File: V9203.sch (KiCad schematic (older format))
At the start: 80 parts, among them J1 RJ45, J10 GS3, J4 Screw_Terminal_1x04, J6 CONN_01X09, J7 GS3, J8 GS3, U1 V9203, Y1 Crystal_GND24

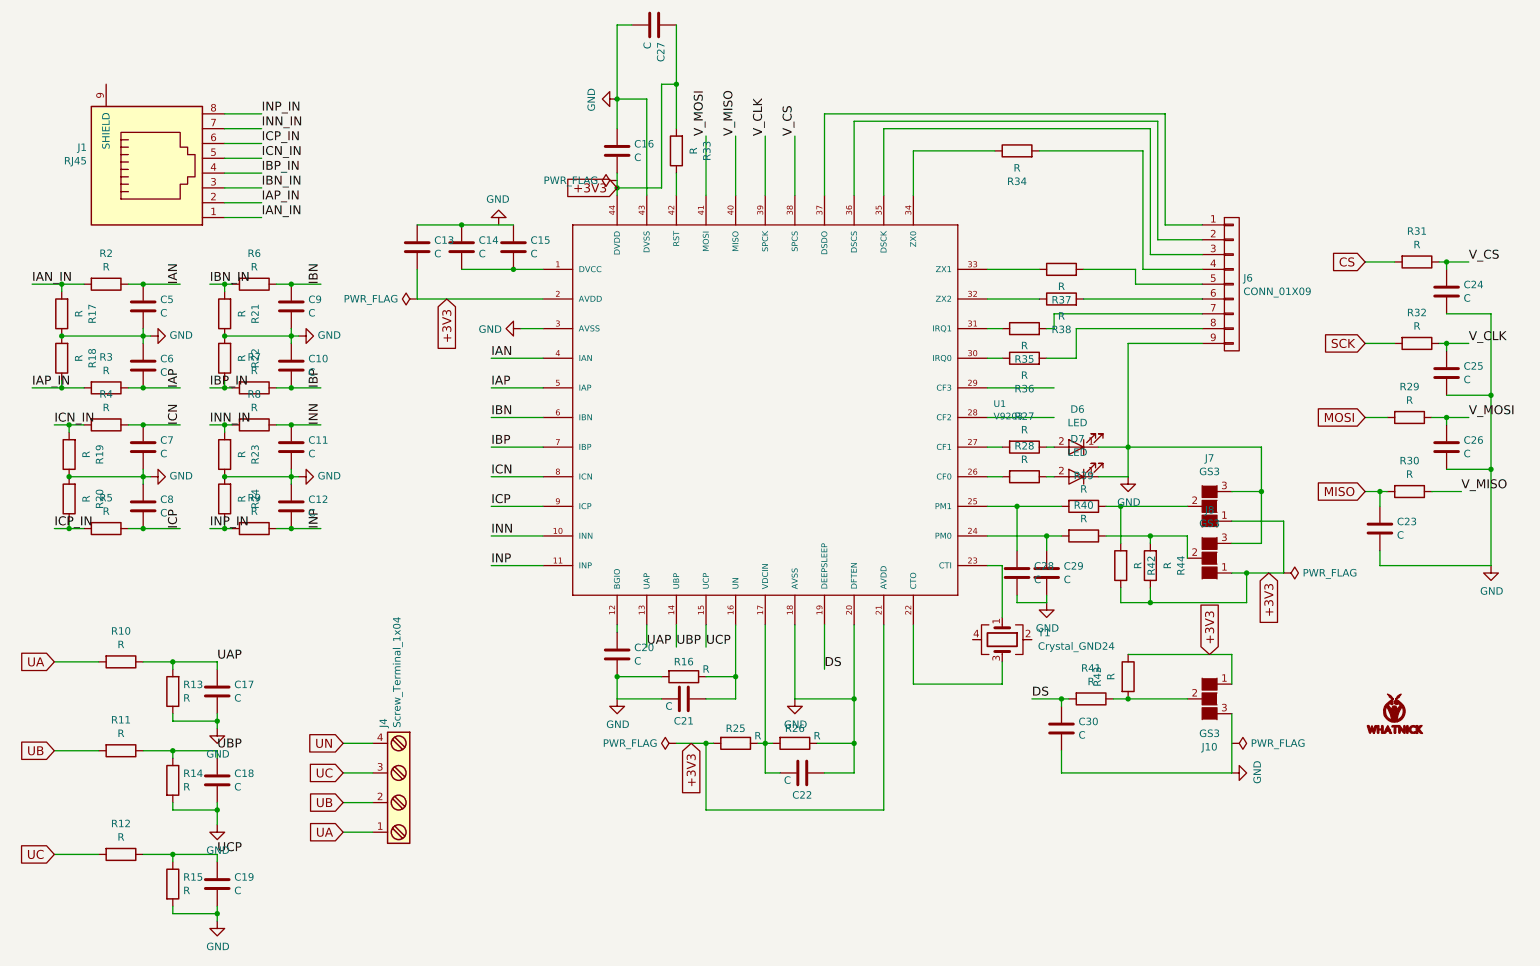
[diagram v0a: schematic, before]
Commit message: Ran ERC and updated pcb
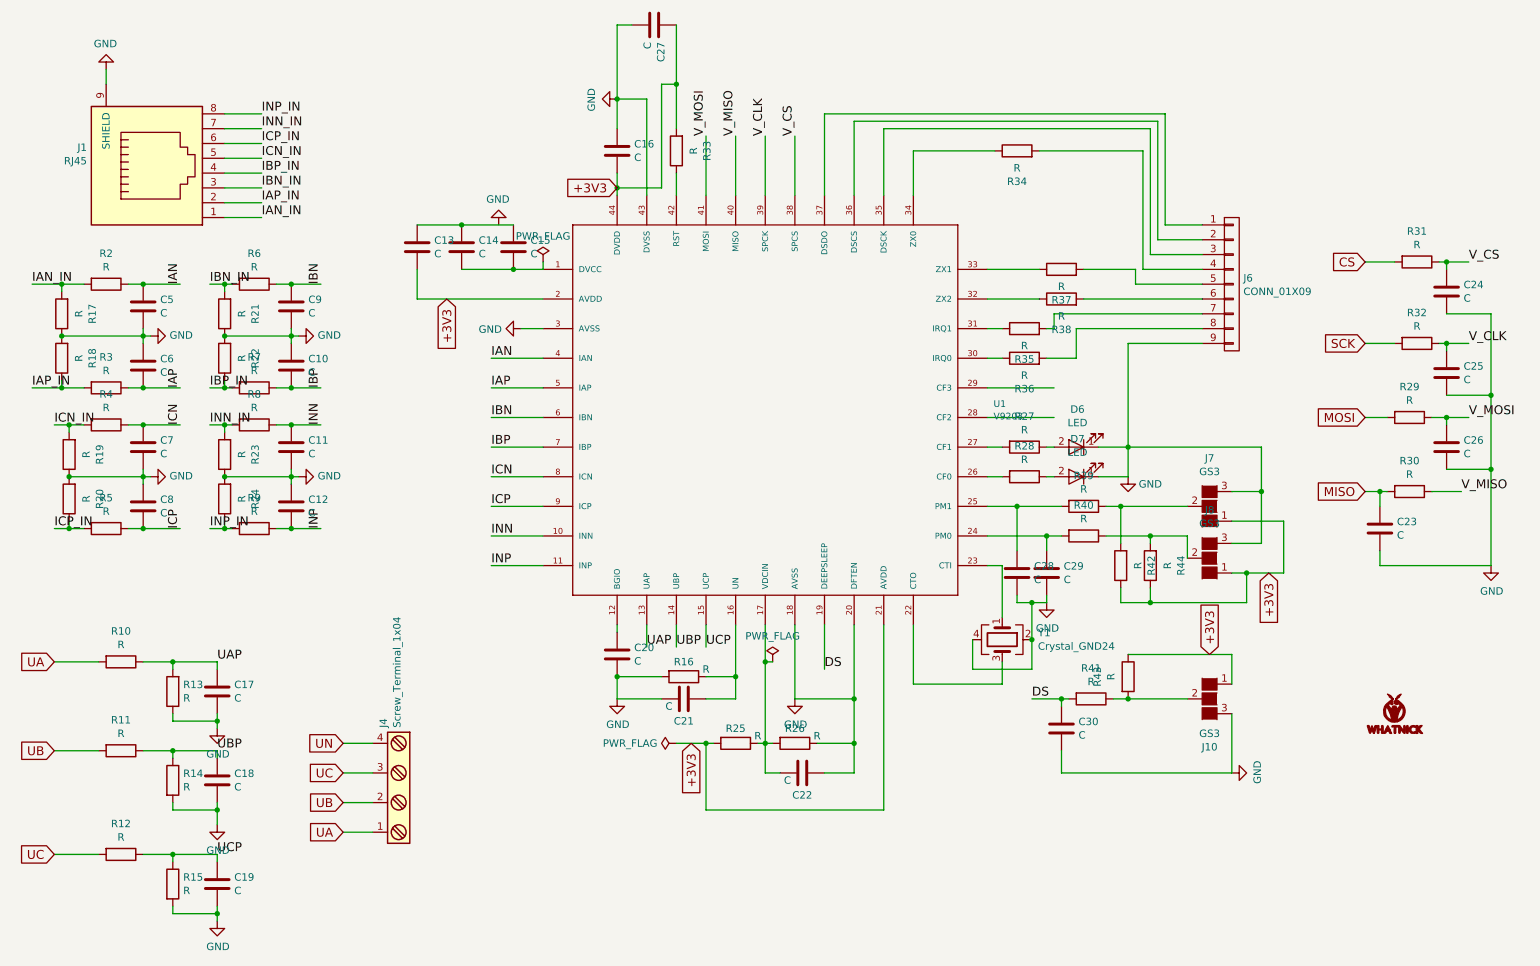
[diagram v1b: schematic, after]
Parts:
- LOGO2: footprint (none) -> Whatnick_logo:Whatnick_logo
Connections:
- net GND: now also J1.9 (SHIELD), Y1.2, Y1.4

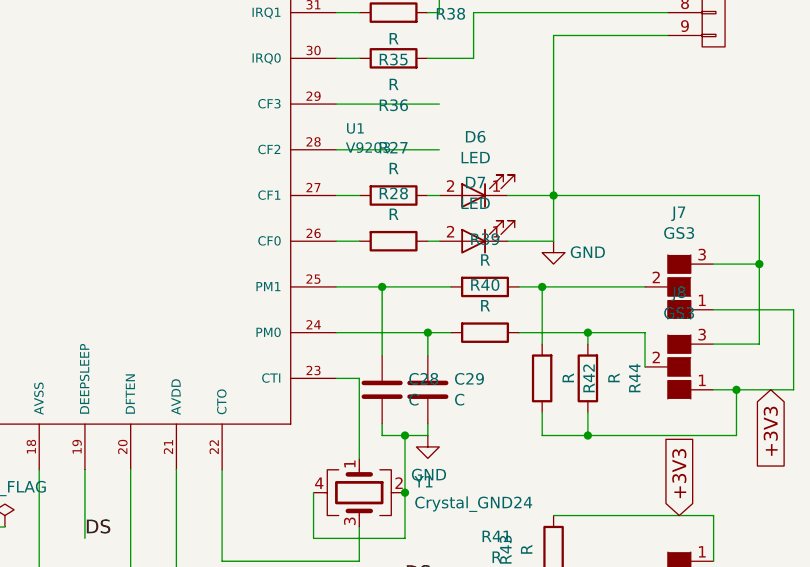
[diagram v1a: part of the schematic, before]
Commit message: Added silk screen markers
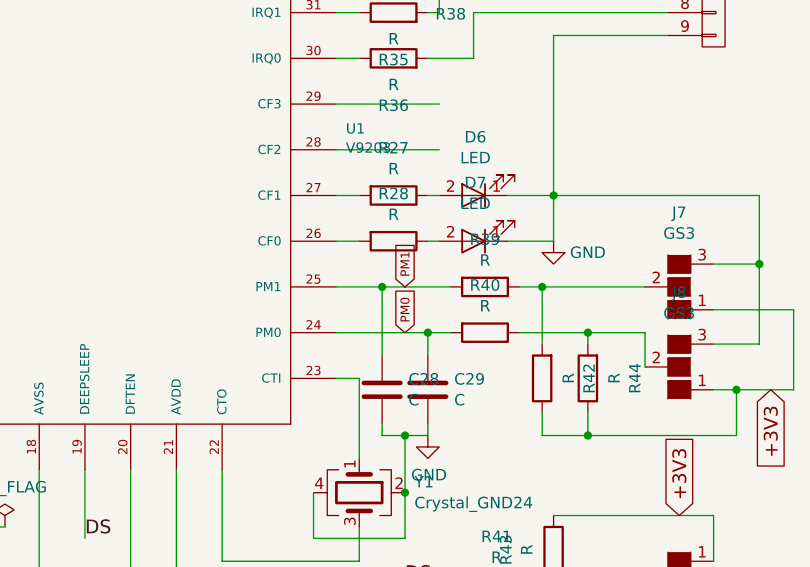
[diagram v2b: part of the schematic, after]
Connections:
- net PM0: now reaches C29.1, R40.2, U1.24 (PM0)
- net PM1: now reaches C28.1, R39.2, U1.25 (PM1)
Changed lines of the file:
@@
 Wire Wire Line
 	1700 6800 1700 6850
+Text GLabel 7500 4100 1    39   Input ~ 0
+PM1
+Text GLabel 7500 4300 1    39   Input ~ 0
+PM0
 $EndSCHEMATC

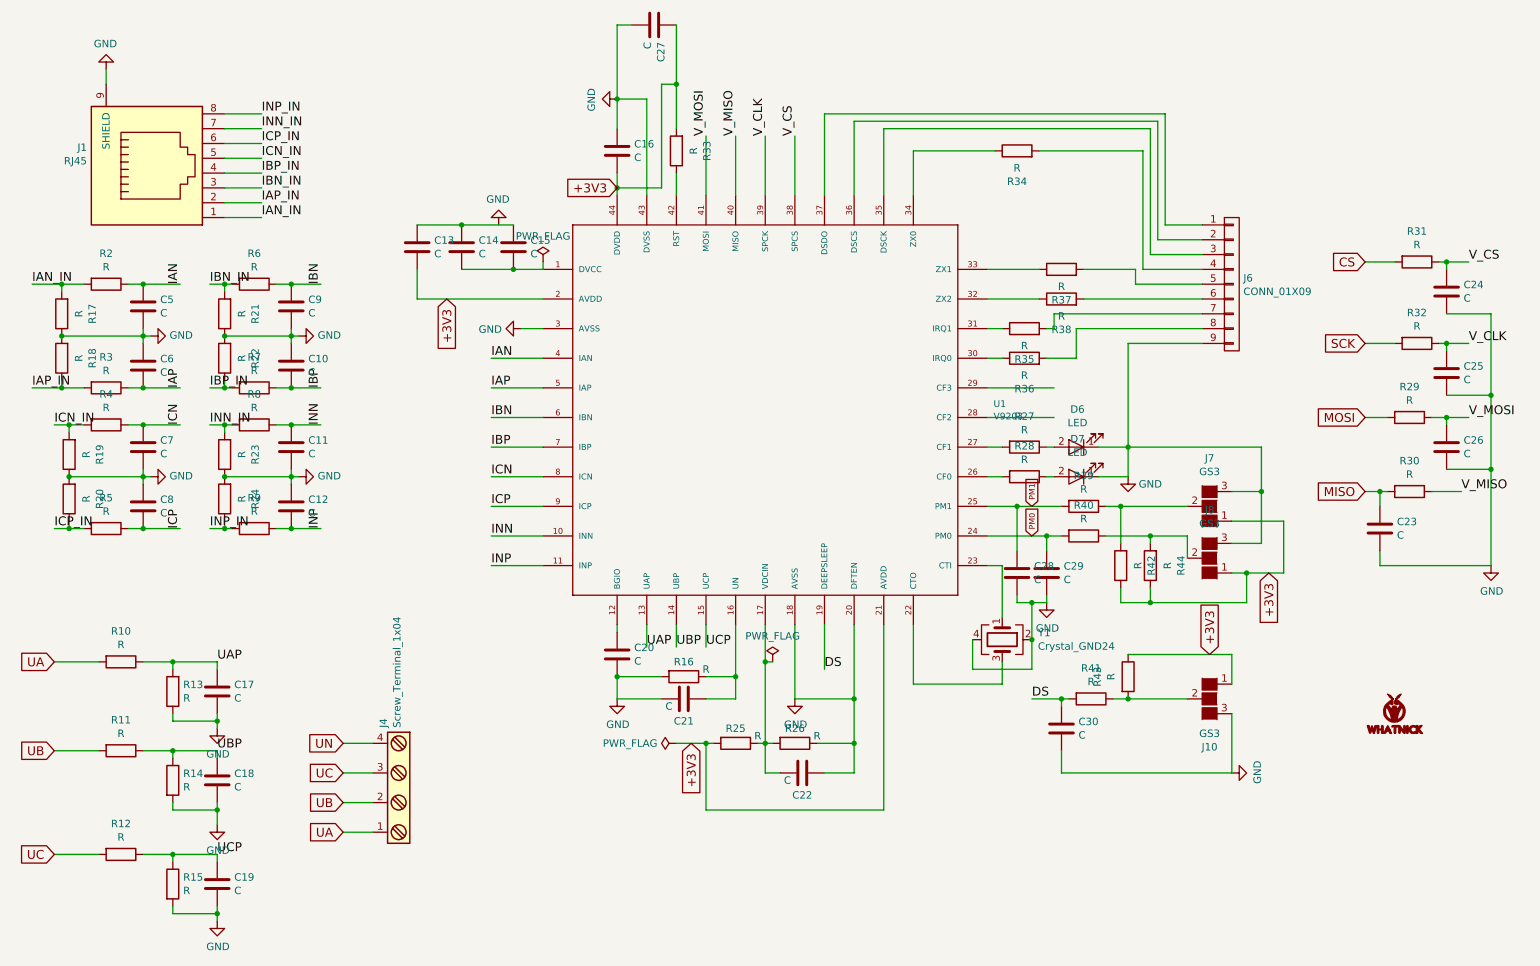
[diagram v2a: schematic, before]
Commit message: Added component values from reference design
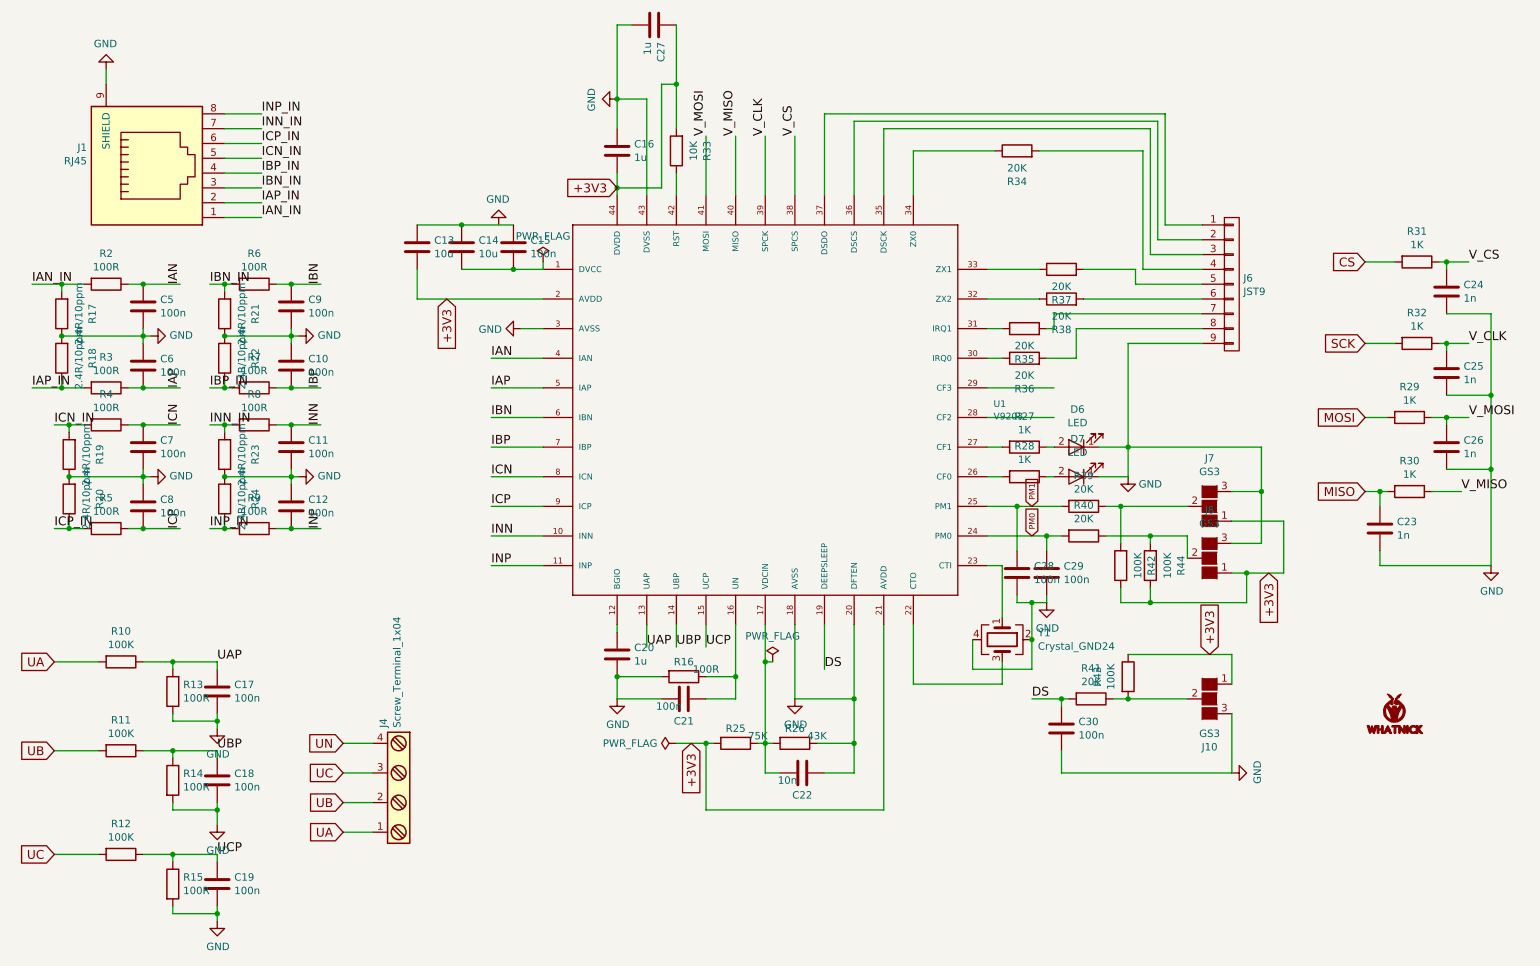
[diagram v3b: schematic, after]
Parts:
- C10, C11, C12, C15, C17, C18, C19, C21, C28, C29, C30, C5, C6, C7, C8, C9: value C -> 100n
- C13, C14: value C -> 10u
- C16, C20, C27: value C -> 1u
- C22: value C -> 10n
- C23, C24, C25, C26: value C -> 1n
- J6: value CONN_01X09 -> JST9
- LOGO2: manf# Value -> (none)
- R10, R11, R12: value R -> 100K; manf# (none) -> Value
- R13, R14, R15: value R -> 100R; manf# (none) -> Value
- R16, R2, R3, R4, R5, R6, R7, R8, R9: value R -> 100R
- R17, R18, R19, R20, R21, R22, R23, R24: value R -> 2.4R/10ppm
- R25: value R -> 75K
- R26: value R -> 43K
- R27, R28, R29, R30, R31, R32: value R -> 1K
- R33: value R -> 10K
- R34, R35, R36, R37, R38, R39, R40, R41: value R -> 20K
- R42, R43, R44: value R -> 100K

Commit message: Started adding part numbers
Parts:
- C16: manf# (none) -> 04026D105KAT2A
- C24: manf# (none) -> 04025C102KAT2A
- C5: manf# (none) -> 0402YD104KAT2A
- J1: manf# (none) -> 95540-2881
- R6: manf# (none) -> CR0402-FX-1000GLF
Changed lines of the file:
@@
 F 2 "Molex_RJ45:RJ45_8" H -50 400 50  0001 C CNN
 F 3 "" H -50 400 50  0001 C CNN
+F 4 "95540-2881" H 1600 1800 60  0001 C CNN "manf#"
 	1    1600 1800
 	0    -1   -1   0
@@
 F 2 "Capacitors_SMD:C_0402" H -62 -350 50  0001 C CNN
 F 3 "" H -100 -200 50  0001 C CNN
+F 4 "0402YD104KAT2A" H 1500 2750 60  0001 C CNN "manf#"
 	1    1500 2750
 	1    0    0    -1
@@
 F 2 "Resistors_SMD:R_0402" V -370 450 50  0001 C CNN
 F 3 "" H -300 450 50  0001 C CNN
+F 4 "CR0402-FX-1000GLF" H 2250 2600 60  0001 C CNN "manf#"
 	1    2250 2600
 	0    1    1    0
@@
 F 2 "Capacitors_SMD:C_0402" H 3138 -1400 50  0001 C CNN
 F 3 "" H 3100 -1250 50  0001 C CNN
+F 4 "04026D105KAT2A" H 4700 1700 60  0001 C CNN "manf#"
 	1    4700 1700
 	-1   0    0    1
@@
 F 2 "Capacitors_SMD:C_0402" H 8738 -450 50  0001 C CNN
 F 3 "" H 8700 -300 50  0001 C CNN
+F 4 "04025C102KAT2A" H 10300 2650 60  0001 C CNN "manf#"
 	1    10300 2650
 	1    0    0    -1

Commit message: Added more part numbers
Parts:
- C14: manf# (none) -> T491A106K016AT
- C22: manf# (none) -> 0402YC103KAT2A
- R10: manf# Value -> RG1608P-104-B
- R25: manf# (none) -> CPF0402B75KE1
- R26: manf# (none) -> CPF0402B43KE
- R29: manf# (none) -> CRCW04021K00FKED
- R33: manf# (none) -> CRCW040210K0FKED
- R34: manf# (none) -> CRCW040220K0FKED
- R42: manf# (none) -> CRCW0402100KFKED
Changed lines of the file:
@@
 F 2 "Capacitors_Tantalum_SMD:CP_Tantalum_Case-A_EIA-3216-18_Reflow" H 2088 -750 50  0001 C CNN
 F 3 "" H 2050 -600 50  0001 C CNN
+F 4 "T491A106K016AT" H 3650 2350 60  0001 C CNN "manf#"
 	1    3650 2350
 	1    0    0    -1
@@
 F 2 "Resistors_SMD:R_0603_HandSoldering" V -1270 3000 50  0001 C CNN
 F 3 "" H -1200 3000 50  0001 C CNN
-F 4 "Value" H 1350 5150 60  0001 C CNN "manf#"
+F 4 "RG1608P-104-B" H 1350 5150 60  0001 C CNN "manf#"
 	1    1350 5150
 	0    1    1    0
@@
 F 2 "Resistors_SMD:R_0402" V 2880 3550 50  0001 C CNN
 F 3 "" H 2950 3550 50  0001 C CNN
+F 4 "CPF0402B75KE1" H 5500 5700 60  0001 C CNN "manf#"
 	1    5500 5700
 	0    1    1    0
@@
 F 2 "Resistors_SMD:R_0402" V 3280 3550 50  0001 C CNN
 F 3 "" H 3350 3550 50  0001 C CNN
+F 4 "CPF0402B43KE" H 5900 5700 60  0001 C CNN "manf#"
 	1    5900 5700
 	0    1    1    0
@@
 F 2 "Capacitors_SMD:C_0402" H 4388 2800 50  0001 C CNN
 F 3 "" H 4350 2950 50  0001 C CNN
+F 4 "0402YC103KAT2A" H 5950 5900 60  0001 C CNN "manf#"
 	1    5950 5900
 	0    1    1    0
@@
 F 2 "Resistors_SMD:R_0402" V 7430 1350 50  0001 C CNN
 F 3 "" H 7500 1350 50  0001 C CNN
+F 4 "CRCW04021K00FKED" H 10050 3500 60  0001 C CNN "manf#"
 	1    10050 3500
 	0    1    1    0
@@
 F 2 "Resistors_SMD:R_0402" V 2480 -450 50  0001 C CNN
 F 3 "" H 2550 -450 50  0001 C CNN
+F 4 "CRCW040210K0FKED" H 5100 1700 60  0001 C CNN "manf#"
 	1    5100 1700
 	-1   0    0    1
@@
 F 2 "Resistors_SMD:R_0402" V 4780 -450 50  0001 C CNN
 F 3 "" H 4850 -450 50  0001 C CNN
+F 4 "CRCW040220K0FKED" H 7400 1700 60  0001 C CNN "manf#"
 	1    7400 1700
 	0    -1   -1   0
@@
 F 2 "Resistors_SMD:R_0402" V 5480 2350 50  0001 C CNN
 F 3 "" H 5550 2350 50  0001 C CNN
+F 4 "CRCW0402100KFKED" H 8100 4500 60  0001 C CNN "manf#"
 	1    8100 4500
 	-1   0    0    1

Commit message: Added more part numbers
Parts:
- R11, R12, R13, R14, R15: manf# Value -> (none)
- R17: manf# (none) -> ERJ3BQF2R4V
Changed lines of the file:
@@
 F 2 "Resistors_SMD:R_0402" V -920 3200 50  0001 C CNN
 F 3 "" H -850 3200 50  0001 C CNN
-F 4 "Value" H 1700 5350 60  0001 C CNN "manf#"
+F 4 "" H 1700 5350 60  0001 C CNN "manf#"
 	1    1700 5350
 	-1   0    0    1
@@
 F 2 "Resistors_SMD:R_0603_HandSoldering" V -1270 3600 50  0001 C CNN
 F 3 "" H -1200 3600 50  0001 C CNN
-F 4 "Value" H 1350 5750 60  0001 C CNN "manf#"
+F 4 "" H 1350 5750 60  0001 C CNN "manf#"
 	1    1350 5750
 	0    1    1    0
@@
 F 2 "Resistors_SMD:R_0402" V -920 3800 50  0001 C CNN
 F 3 "" H -850 3800 50  0001 C CNN
-F 4 "Value" H 1700 5950 60  0001 C CNN "manf#"
+F 4 "" H 1700 5950 60  0001 C CNN "manf#"
 	1    1700 5950
 	1    0    0    -1
@@
 F 2 "Resistors_SMD:R_0603_HandSoldering" V -1270 4300 50  0001 C CNN
 F 3 "" H -1200 4300 50  0001 C CNN
-F 4 "Value" H 1350 6450 60  0001 C CNN "manf#"
+F 4 "" H 1350 6450 60  0001 C CNN "manf#"
 	1    1350 6450
 	0    1    1    0
@@
 F 2 "Resistors_SMD:R_0402" V -920 4500 50  0001 C CNN
 F 3 "" H -850 4500 50  0001 C CNN
-F 4 "Value" H 1700 6650 60  0001 C CNN "manf#"
+F 4 "" H 1700 6650 60  0001 C CNN "manf#"
 	1    1700 6650
 	1    0    0    -1
@@
 F 2 "Resistors_SMD:R_0603" V -1670 650 50  0001 C CNN
 F 3 "" H -1600 650 50  0001 C CNN
+F 4 "ERJ3BQF2R4V" H 950 2800 60  0001 C CNN "manf#"
 	1    950  2800
 	-1   0    0    1
@@
 F 2 "" H 0   50  50  0001 C CNN
 F 3 "" H 0   50  50  0001 C CNN
-F 4 "Value" H 1250 1150 60  0001 C CNN "manf#"
+F 4 "" H 1250 1150 60  0001 C CNN "manf#"
 	1    1250 1150
 	-1   0    0    1

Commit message: More part numbers
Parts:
- U1: kicost:pricing (none) -> 1:$5;10:$4;100:$3
- Y1: kicost:pricing (none) -> 1:$3.00;10:$2.85
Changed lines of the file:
@@
 F 2 "Housings_QFP:TQFP-44_10x10mm_Pitch0.8mm" H 1750 1250 60  0001 C CNN
 F 3 "" H 1750 1250 60  0001 C CNN
+F 4 "1:$5;10:$4;100:$3" H 5500 3400 60  0001 C CNN "kicost:pricing"
 	1    5500 3400
 	1    0    0    -1
@@
 F 2 "Crystals:Crystal_SMD_Abracon_ABM8G-4pin_3.2x2.5mm" H 0   50  50  0001 C CNN
 F 3 "" H 0   50  50  0001 C CNN
+F 4 "1:$3.00;10:$2.85" V 7300 5000 60  0001 C CNN "kicost:pricing"
 	1    7300 5000
 	0    1    1    0

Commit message: JST parts
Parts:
- J6: manf# (none) -> SM09B-SRSS-TB(LF)(SN)
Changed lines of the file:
@@
 F 2 "Connectors_JST:JST_SH_SM09B-SRSS-TB_09x1.00mm_Angled" H 0   500 50  0001 C CNN
 F 3 "" H 0   500 50  0001 C CNN
+F 4 "SM09B-SRSS-TB(LF)(SN)" H 8850 2600 60  0001 C CNN "manf#"
 	1    8850 2600
 	1    0    0    -1
